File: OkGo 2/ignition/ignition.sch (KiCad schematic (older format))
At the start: 42 parts, among them P101 JST_XH_F, P102 JST_XH_M, P103 CHARGE_CASE, P104 BATT, P105 BATT, P106 SMA, P107 ARM_LED, P108 ARM_LED, SW101 20A ROCKER, U101 CLIP, U102 FUSE 15A, U103 SWD, U104 BEZEL, U105 RFM95W, U106 STM32F071CBT6, U107 TSR 0.5-2433, Y101 8MHz

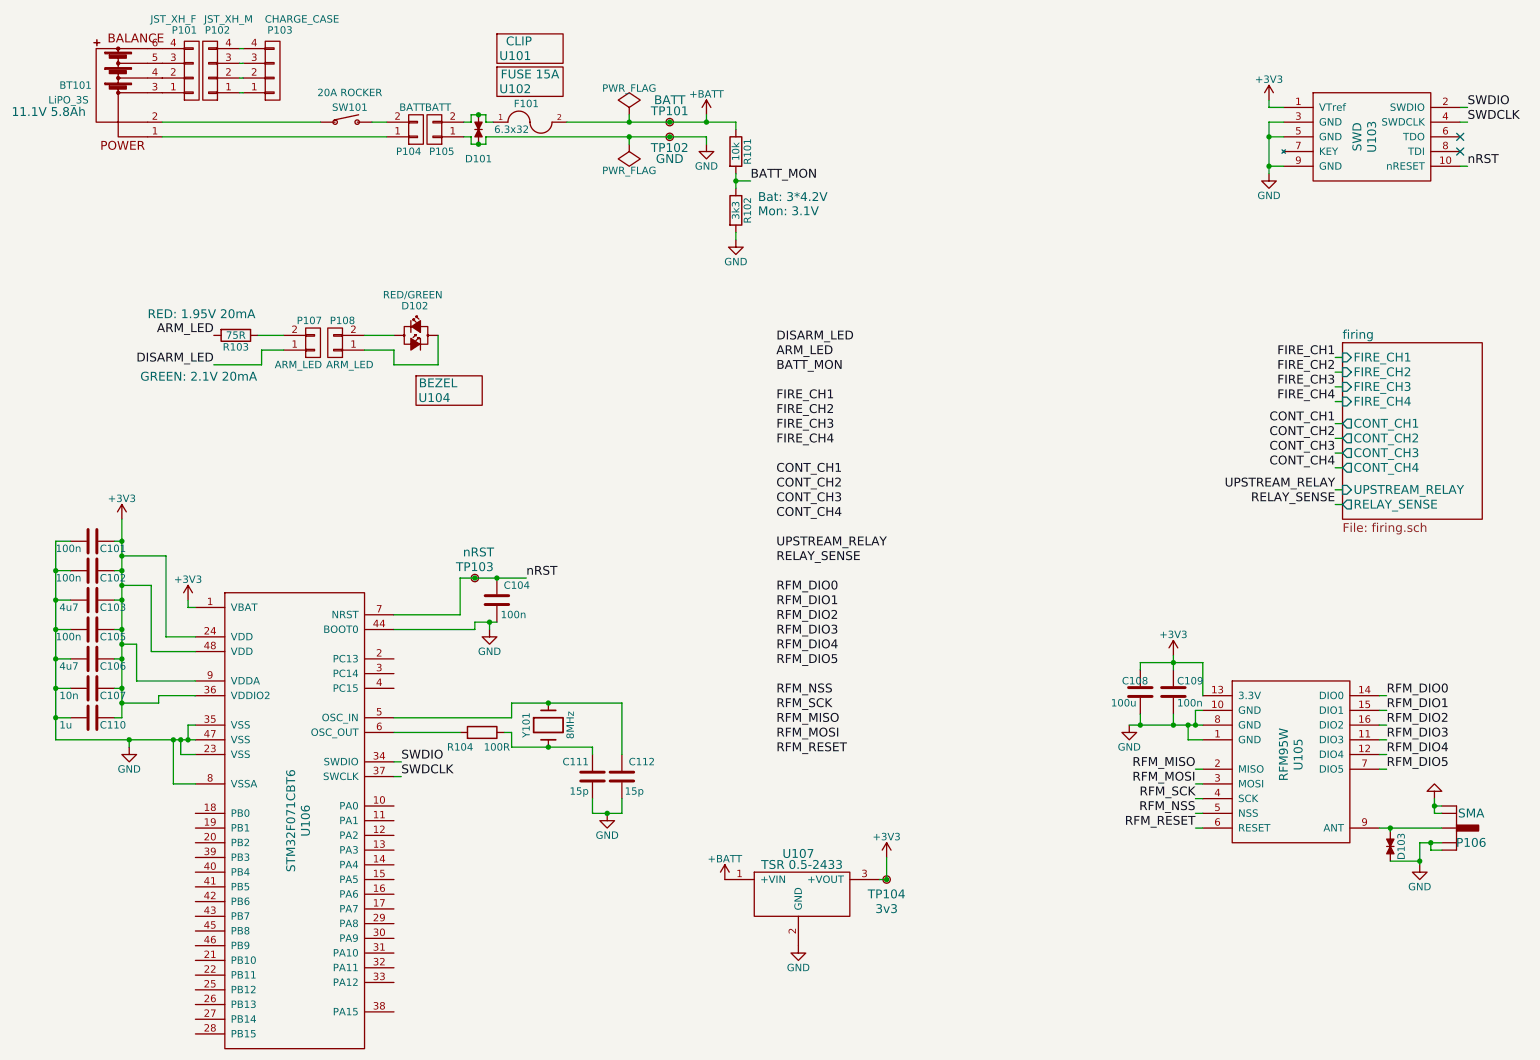
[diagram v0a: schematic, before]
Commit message: Provisional first place+pinassign+route of ignition
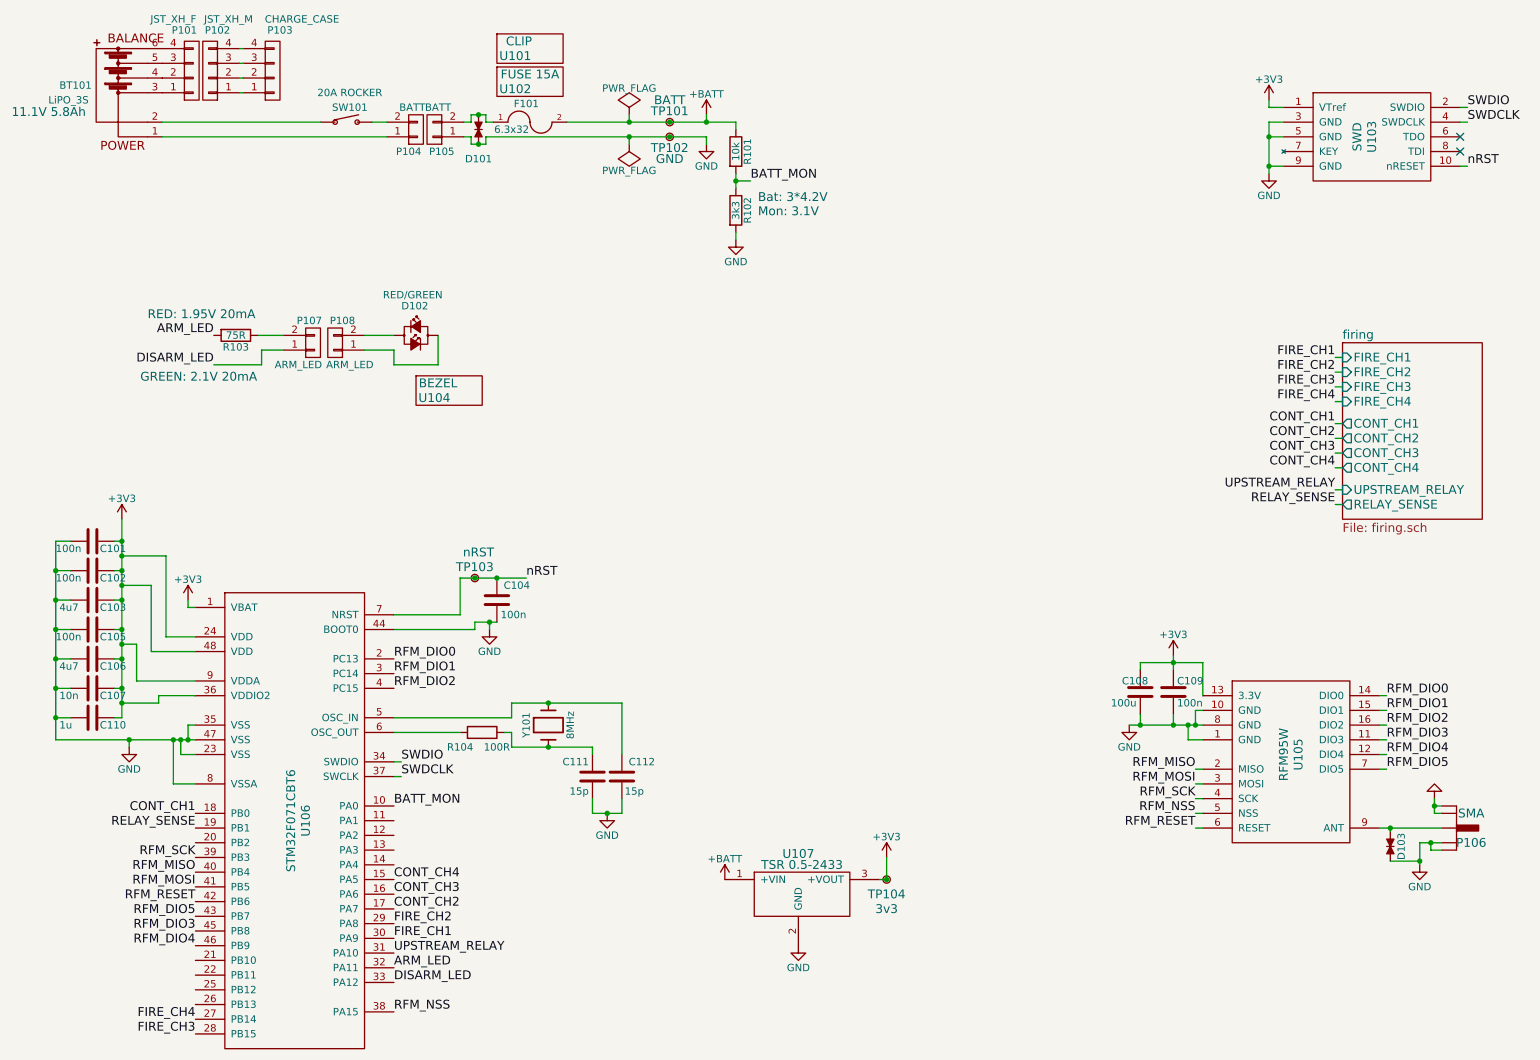
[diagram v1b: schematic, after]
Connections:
- net ARM_LED: now also U106.32 (PA11)
- net BATT_MON: now also U106.10 (PA0)
- net CONT_CH1: now also U106.18 (PB0)
- net CONT_CH2: now also U106.17 (PA7)
- net CONT_CH3: now also U106.16 (PA6)
- net CONT_CH4: now also U106.15 (PA5)
- net DISARM_LED: now also U106.33 (PA12)
- net FIRE_CH1: now also U106.30 (PA9)
- net FIRE_CH2: now also U106.29 (PA8)
- net FIRE_CH3: now also U106.28 (PB15)
- net FIRE_CH4: now also U106.27 (PB14)
- net RELAY_SENSE: now also U106.19 (PB1)
- net RFM_DIO0: now also U106.2 (PC13)
- net RFM_DIO1: now also U106.3 (PC14)
- net RFM_DIO2: now also U106.4 (PC15)
- net RFM_DIO3: now also U106.45 (PB8)
- net RFM_DIO4: now also U106.46 (PB9)
- net RFM_DIO5: now also U106.43 (PB7)
- net RFM_MISO: now also U106.40 (PB4)
- net RFM_MOSI: now also U106.41 (PB5)
- net RFM_NSS: now also U106.38 (PA15)
- net RFM_RESET: now also U106.42 (PB6)
- net RFM_SCK: now also U106.39 (PB3)
- net UPSTREAM_RELAY: now also U106.31 (PA10)
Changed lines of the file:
@@
 F 1 "STM32F071CBT6" V 2600 6300 60  0000 C CNN
 F 2 "Housings_QFP:LQFP-48_7x7mm_Pitch0.5mm" H 2650 6350 60  0001 C CNN
-F 3 "" H 2650 6350 60  0000 C CNN
+F 3 "http://www.st.com/st-web-ui/static/active/en/resource/technical/document/datasheet/DM00098745.pdf" H 2650 6350 60  0001 C CNN
 F 4 "2432093" H 2650 6150 60  0001 C CNN "Farnell"
 	1    2650 6150
@@
 Text Label 9700 3850 2    60   ~ 0
 RELAY_SENSE
-Text Label 5900 3150 0    60   ~ 0
+Text Label 3300 6800 0    60   ~ 0
 FIRE_CH1
-Text Label 5900 3250 0    60   ~ 0
+Text Label 3300 6700 0    60   ~ 0
 FIRE_CH2
-Text Label 5900 3350 0    60   ~ 0
+Text Label 1950 7450 2    60   ~ 0
 FIRE_CH3
-Text Label 5900 3450 0    60   ~ 0
+Text Label 1950 7350 2    60   ~ 0
 FIRE_CH4
-Text Label 5900 3650 0    60   ~ 0
+Text Label 1950 5950 2    60   ~ 0
 CONT_CH1
-Text Label 5900 3750 0    60   ~ 0
+Text Label 3300 6600 0    60   ~ 0
 CONT_CH2
-Text Label 5900 3850 0    60   ~ 0
+Text Label 3300 6500 0    60   ~ 0
 CONT_CH3
-Text Label 5900 3950 0    60   ~ 0
+Text Label 3300 6400 0    60   ~ 0
 CONT_CH4
-Text Label 5900 4150 0    60   ~ 0
+Text Label 3300 6900 0    60   ~ 0
 UPSTREAM_RELAY
-Text Label 5900 4250 0    60   ~ 0
+Text Label 1950 6050 2    60   ~ 0
 RELAY_SENSE
 Text Label 3350 5600 0    60   ~ 0
@@
 Text Label 5725 1650 0    60   ~ 0
 BATT_MON
-Text Label 5900 2950 0    60   ~ 0
+Text Label 3300 5900 0    60   ~ 0
 BATT_MON
 Text Label 10050 5150 0    60   ~ 0
@@
 Text Label 8750 6050 2    60   ~ 0
 RFM_RESET
-Text Label 5900 4450 0    60   ~ 0
+Text Label 3300 4900 0    60   ~ 0
 RFM_DIO0
-Text Label 5900 4550 0    60   ~ 0
+Text Label 3300 5000 0    60   ~ 0
 RFM_DIO1
-Text Label 5900 4650 0    60   ~ 0
+Text Label 3300 5100 0    60   ~ 0
 RFM_DIO2
-Text Label 5900 4750 0    60   ~ 0
+Text Label 1950 6750 2    60   ~ 0
 RFM_DIO3
-Text Label 5900 4850 0    60   ~ 0
+Text Label 1950 6850 2    60   ~ 0
 RFM_DIO4
-Text Label 5900 4950 0    60   ~ 0
+Text Label 1950 6650 2    60   ~ 0
 RFM_DIO5
-Text Label 5900 5150 0    60   ~ 0
+Text Label 3300 7300 0    60   ~ 0
 RFM_NSS
-Text Label 5900 5250 0    60   ~ 0
+Text Label 1950 6250 2    60   ~ 0
 RFM_SCK
-Text Label 5900 5350 0    60   ~ 0
+Text Label 1950 6350 2    60   ~ 0
 RFM_MISO
-Text Label 5900 5450 0    60   ~ 0
+Text Label 1950 6450 2    60   ~ 0
 RFM_MOSI
-Text Label 5900 5550 0    60   ~ 0
+Text Label 1950 6550 2    60   ~ 0
 RFM_RESET
 Text Label 4200 4350 0    60   ~ 0
@@
 Text Label 2075 2900 2    60   ~ 0
 DISARM_LED
-Text Label 5900 2850 0    60   ~ 0
+Text Label 3300 7000 0    60   ~ 0
 ARM_LED
-Text Label 5900 2750 0    60   ~ 0
+Text Label 3300 7100 0    60   ~ 0
 DISARM_LED
 $Comp

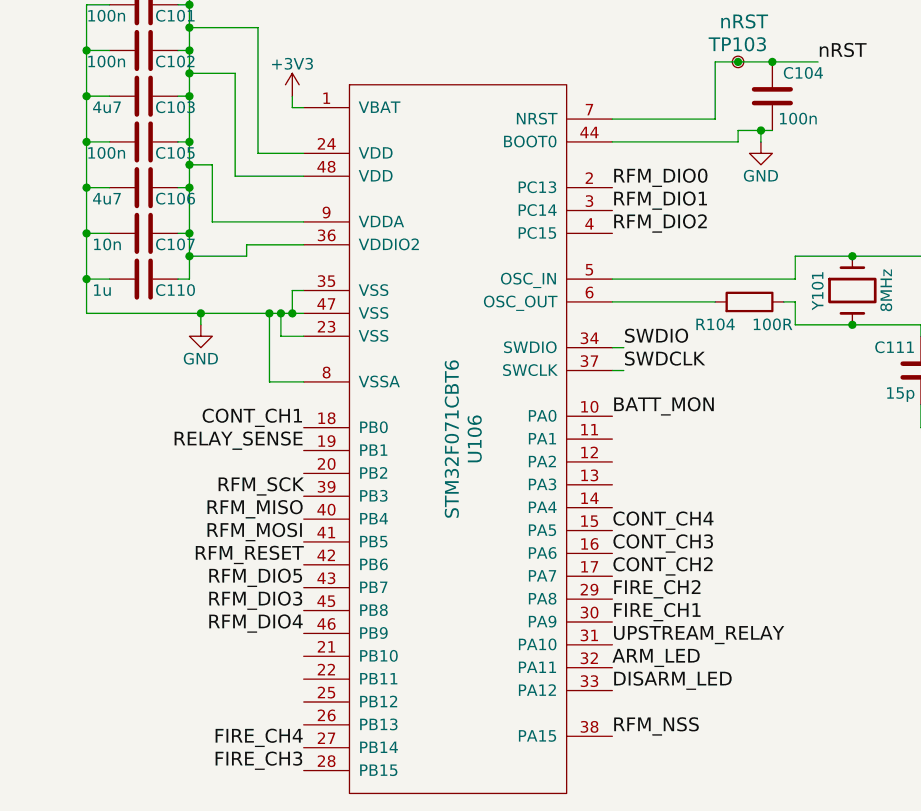
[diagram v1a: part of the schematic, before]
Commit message: Second route of ignition
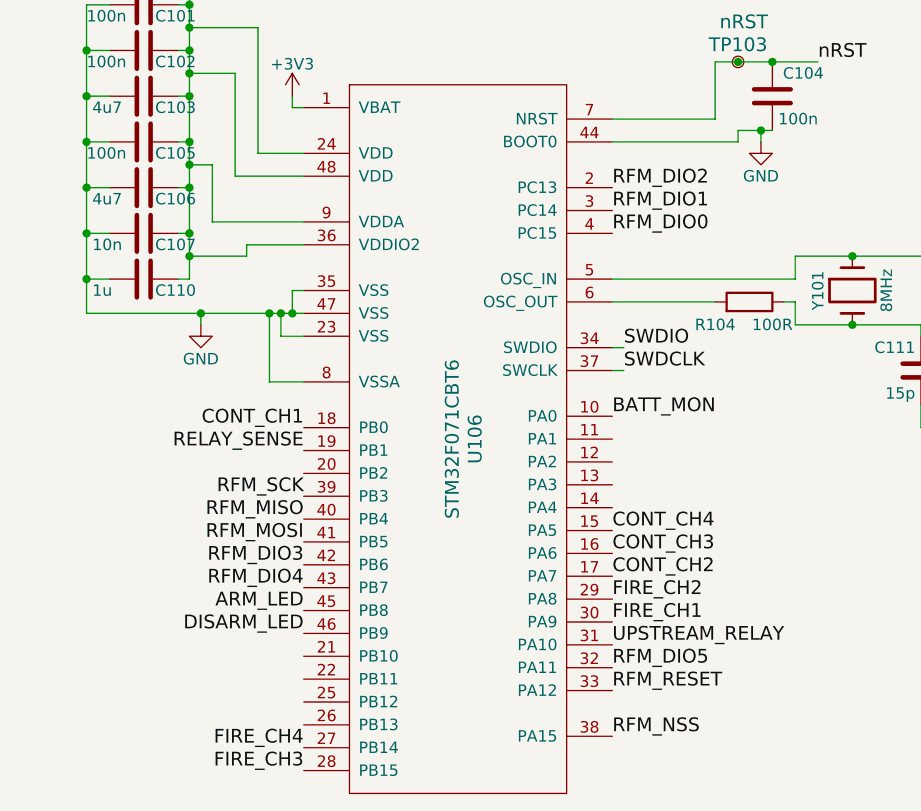
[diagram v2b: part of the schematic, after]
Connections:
- net ARM_LED: now also U106.45 (PB8); no longer U106.32 (PA11)
- net DISARM_LED: now also U106.46 (PB9); no longer U106.33 (PA12)
- net RFM_DIO0: now also U106.4 (PC15); no longer U106.2 (PC13)
- net RFM_DIO2: now also U106.2 (PC13); no longer U106.4 (PC15)
- net RFM_DIO3: now also U106.42 (PB6); no longer U106.45 (PB8)
- net RFM_DIO4: now also U106.43 (PB7); no longer U106.46 (PB9)
- net RFM_DIO5: now also U106.32 (PA11); no longer U106.43 (PB7)
- net RFM_RESET: now also U106.33 (PA12); no longer U106.42 (PB6)
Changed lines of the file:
@@
 Text Label 8750 6050 2    60   ~ 0
 RFM_RESET
-Text Label 3300 4900 0    60   ~ 0
+Text Label 3300 5100 0    60   ~ 0
 RFM_DIO0
 Text Label 3300 5000 0    60   ~ 0
 RFM_DIO1
-Text Label 3300 5100 0    60   ~ 0
+Text Label 3300 4900 0    60   ~ 0
 RFM_DIO2
-Text Label 1950 6750 2    60   ~ 0
+Text Label 1950 6550 2    60   ~ 0
 RFM_DIO3
-Text Label 1950 6850 2    60   ~ 0
+Text Label 1950 6650 2    60   ~ 0
 RFM_DIO4
-Text Label 1950 6650 2    60   ~ 0
+Text Label 3300 7000 0    60   ~ 0
 RFM_DIO5
 Text Label 3300 7300 0    60   ~ 0
@@
 Text Label 1950 6450 2    60   ~ 0
 RFM_MOSI
-Text Label 1950 6550 2    60   ~ 0
+Text Label 3300 7100 0    60   ~ 0
 RFM_RESET
 Text Label 4200 4350 0    60   ~ 0
@@
 Text Label 2075 2900 2    60   ~ 0
 DISARM_LED
-Text Label 3300 7000 0    60   ~ 0
+Text Label 1950 6750 2    60   ~ 0
 ARM_LED
-Text Label 3300 7100 0    60   ~ 0
+Text Label 1950 6850 2    60   ~ 0
 DISARM_LED
 $Comp
